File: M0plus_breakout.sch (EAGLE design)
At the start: 32 parts, among them SW1 SPST_TACT-KMR2, U1 ATSAMD21G-A, U2 SPX3819-3.3, U3 MCP73831T, X1 XTAL_32.768KHZ, X2 microusb

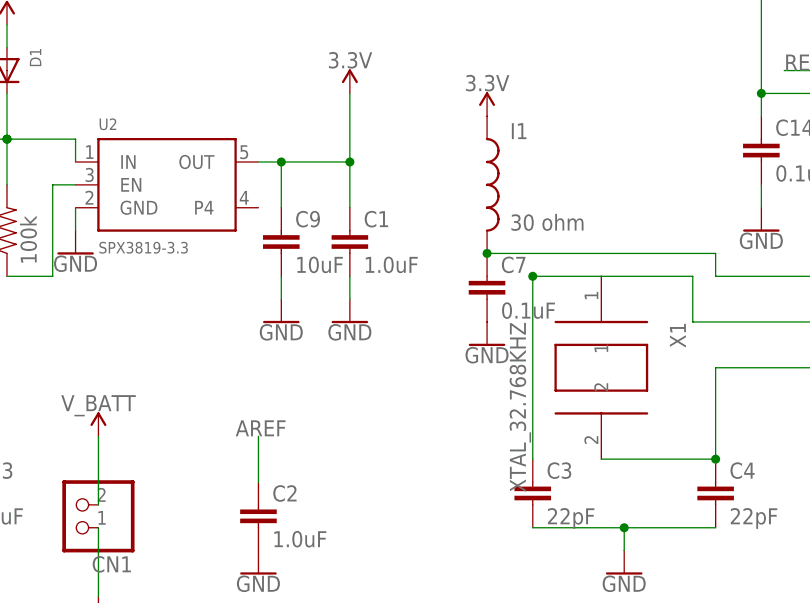
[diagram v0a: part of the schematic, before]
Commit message: added power LED
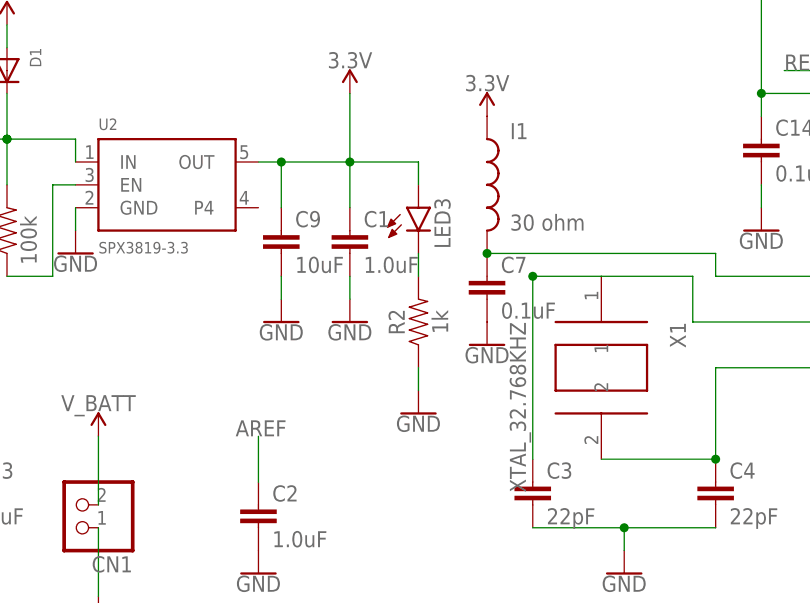
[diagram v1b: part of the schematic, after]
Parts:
- added LED3: (no value), Ilya_Teach:LED0603
- added R2: 1k, SparkFun-Resistors:1KOHM-0603-1/10W-1%
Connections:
- new net N$7: LED3.C, R2.2
- net 3.3V: now also LED3.A
- net GND: now also R2.1
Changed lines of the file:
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@@
 <part name="GND2" library="SparkFun-PowerSymbols" deviceset="GND" device=""/>
 <part name="FRAME1" library="frames" deviceset="A4L-LOC" device="" value="Hello"/>
+<part name="LED3" library="Ilya_Teach" deviceset="LED" device="0603"/>
+<part name="R2" library="SparkFun-Resistors" deviceset="1KOHM" device="-0603-1/10W-1%" value="1k"/>
+<part name="GND19" library="SparkFun-PowerSymbols" deviceset="GND" device=""/>
 </parts>
 <sheets>
@@
 <instance part="GND2" gate="1" x="-25.4" y="-45.72"/>
 <instance part="FRAME1" gate="G$1" x="-78.74" y="-60.96"/>
+<instance part="LED3" gate="G$1" x="-5.08" y="48.26"/>
+<instance part="R2" gate="G$1" x="-5.08" y="35.56" rot="R90"/>
+<instance part="GND19" gate="1" x="-5.08" y="25.4"/>
 </instances>
 <busses>
@@
 <wire x1="-25.4" y1="-40.64" x2="-25.4" y2="-43.18" width="0.1524" layer="91"/>
 </segment>
+<segment>
+<pinref part="GND19" gate="1" pin="GND"/>
+<pinref part="R2" gate="G$1" pin="1"/>
+<wire x1="-5.08" y1="27.94" x2="-5.08" y2="30.48" width="0.1524" layer="91"/>
+</segment>
 </net>
 <net name="N$2" class="0">
@@
 <junction x="-20.32" y="53.34"/>
 <pinref part="C1" gate="G$1" pin="1"/>
+<pinref part="LED3" gate="G$1" pin="A"/>
+<wire x1="-5.08" y1="50.8" x2="-5.08" y2="53.34" width="0.1524" layer="91"/>
+<wire x1="-5.08" y1="53.34" x2="-12.7" y2="53.34" width="0.1524" layer="91"/>
 </segment>
 <segment>
@@
 </segment>
 </net>
+<net name="N$7" class="0">
+<segment>
+<pinref part="R2" gate="G$1" pin="2"/>
+<pinref part="LED3" gate="G$1" pin="C"/>
+<wire x1="-5.08" y1="40.64" x2="-5.08" y2="43.18" width="0.1524" layer="91"/>
+</segment>
+</net>
